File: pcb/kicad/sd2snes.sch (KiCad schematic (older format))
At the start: 0 parts

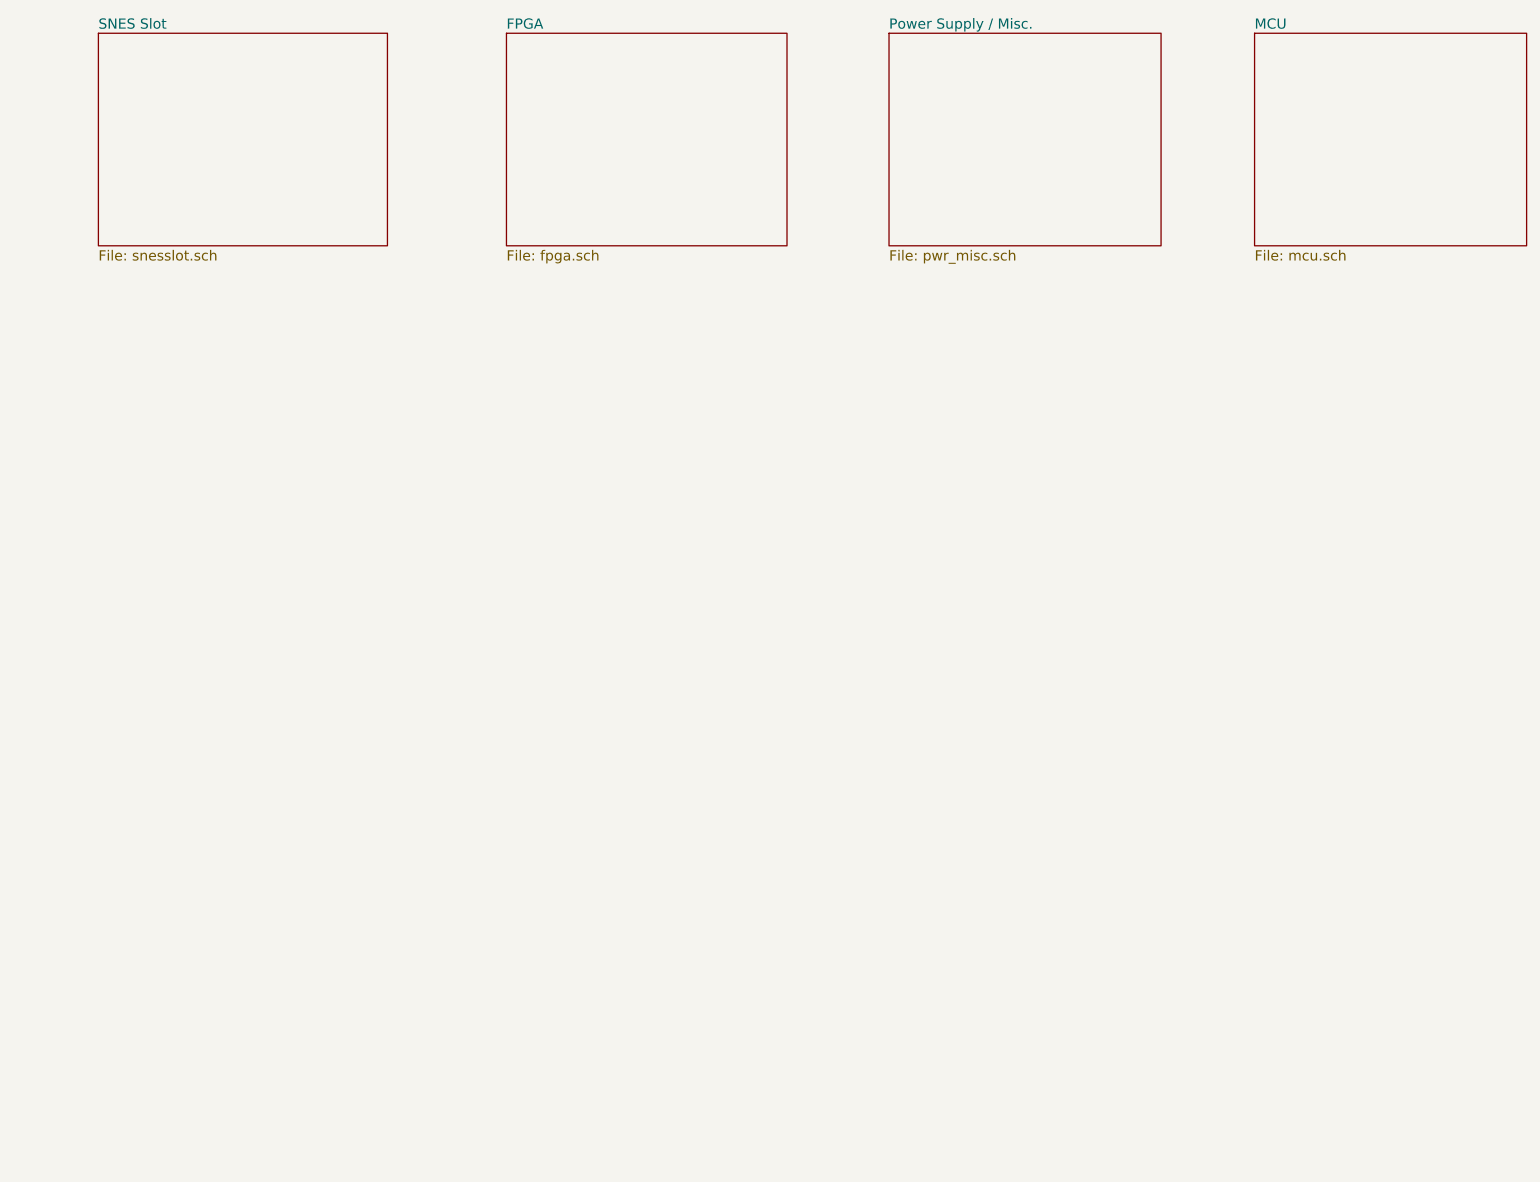
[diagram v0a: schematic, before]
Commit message: clean up AVR code(deprecated), kicad libs, pcb WIP
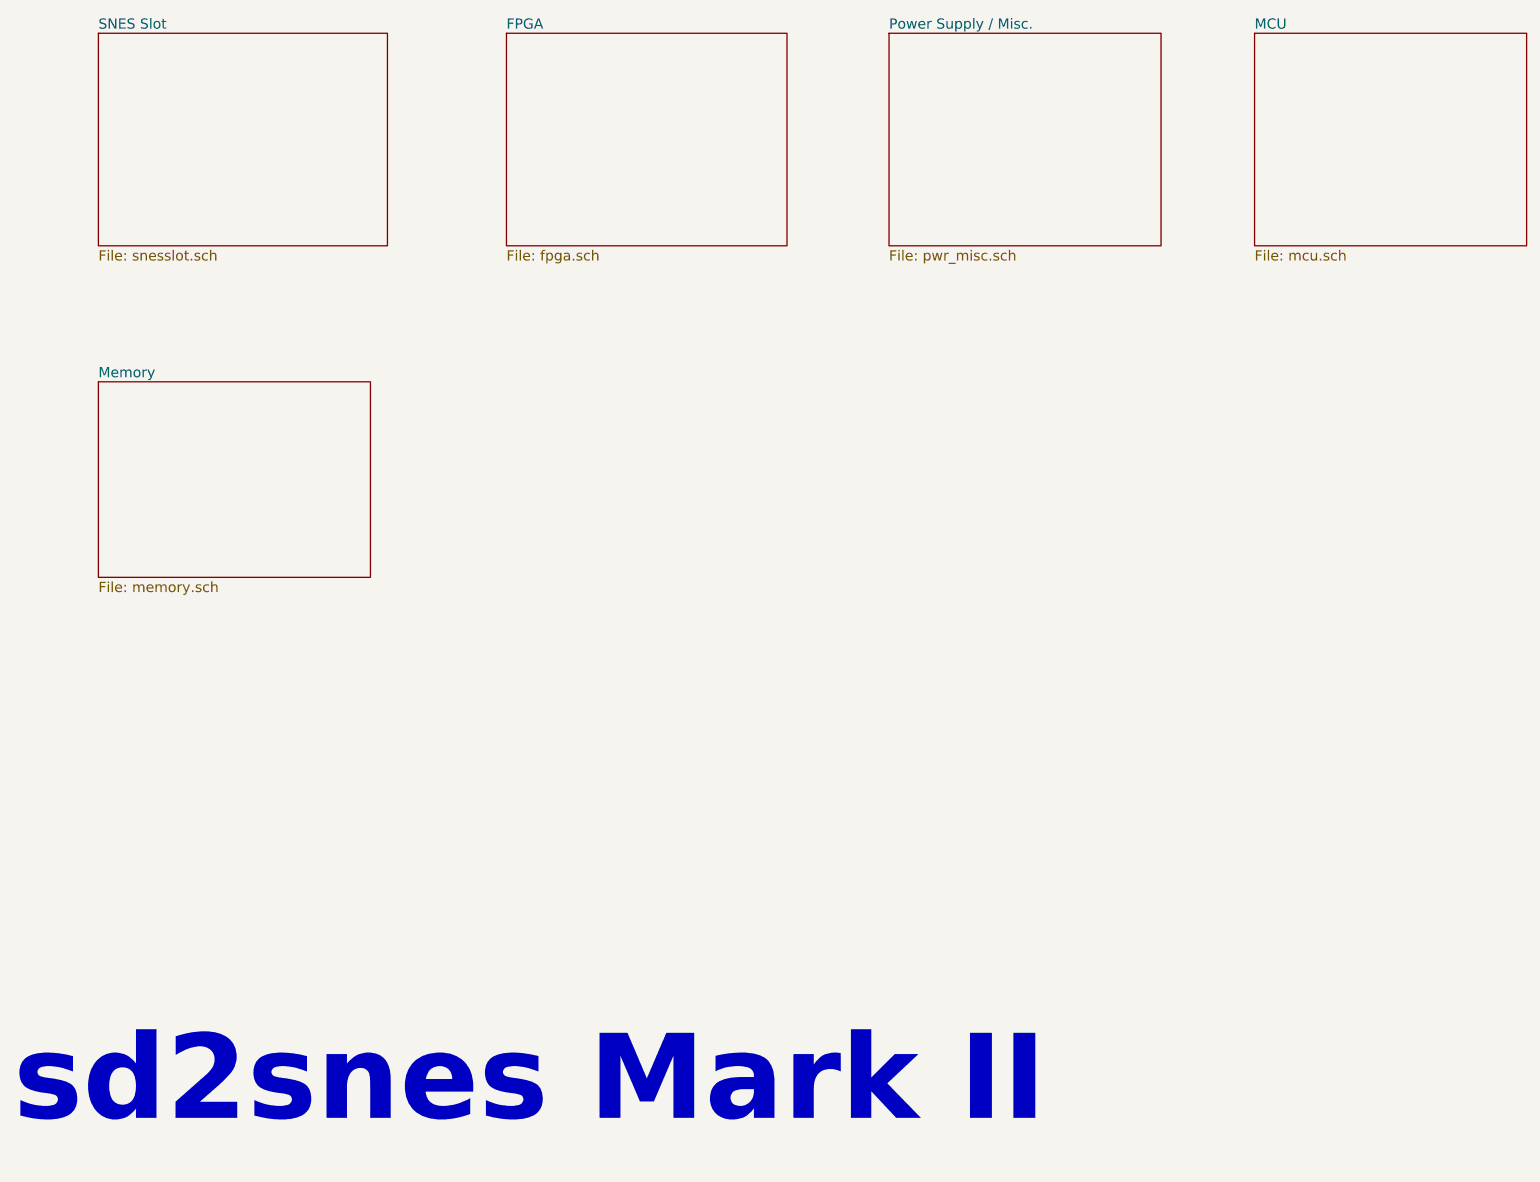
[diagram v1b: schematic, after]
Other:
- note added: "sd2snes Mark II"
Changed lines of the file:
@@
-EESchema Schematic File Version 2  date Tue 09 Feb 2010 11:25:34 PM CET
+EESchema Schematic File Version 2  date Wed 24 Mar 2010 11:33:24 PM CET
 LIBS:sd2snes-cache
 LIBS:power
@@
 LIBS:lpc1754
 LIBS:sdcard
-LIBS:testsw
+LIBS:sd_card
+LIBS:cy62148ev30
+LIBS:mt45w8mw16
+LIBS:cs4344
 EELAYER 24  0
 EELAYER END
 $Descr A4 11700 8267
-Sheet 1 5
+Sheet 1 6
 Title "sd2snes Mark II"
 Date "9 feb 2010"
@@
 Comment4 ""
 $EndDescr
+Text Notes 750  7700 0    500  ~ 100
+sd2snes Mark II
+$Sheet
+S 1250 3300 1600 1150
+U 4BAA6ABD
+F0 "Memory" 60
+F1 "memory.sch" 60
+$EndSheet
 $Sheet
 S 8050 1250 1600 1250
